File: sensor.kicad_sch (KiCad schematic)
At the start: 1 part, among them U301 AS7341DLG

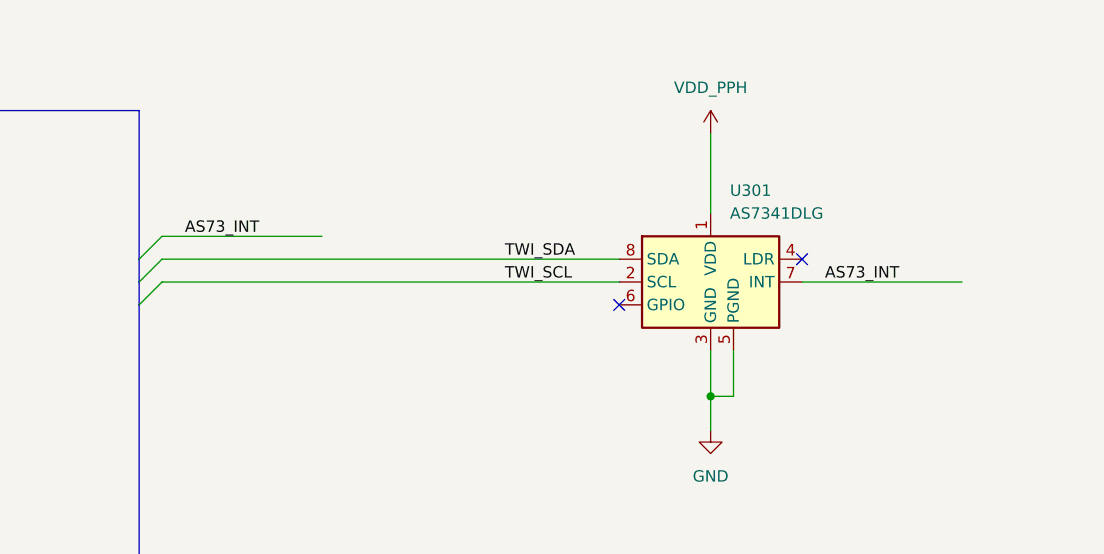
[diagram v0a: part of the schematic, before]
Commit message: Update Schematics - Add footprint to symbols.
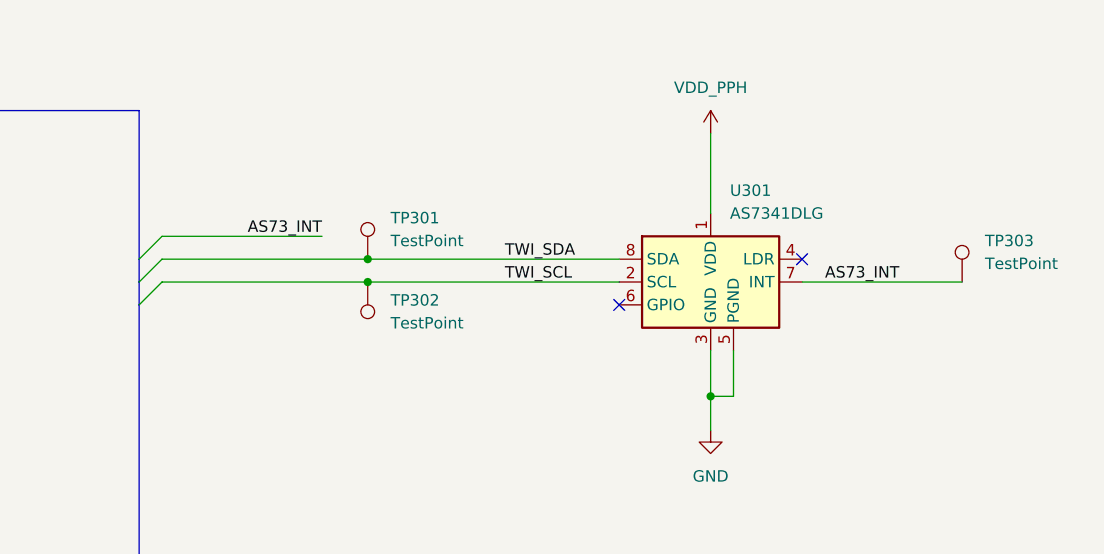
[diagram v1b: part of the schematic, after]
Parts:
- added TP301, TP302, TP303: TestPoint, TestPoint:TestPoint_Keystone_5005-5009_Compact, symbol Connector:TestPoint
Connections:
- net AS73_INT: now also TP303.1
- net TWI_SCL: now also TP302.1
- net TWI_SDA: now also TP301.1
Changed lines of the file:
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@@
+		(color 0 0 0 0)
+	)
+	(junction
+		(at 101.6 57.15)
+		(diameter 0)
+		(color 0 0 0 0)
+	)
+	(junction
+		(at 101.6 54.61)
+		(diameter 0)
 		(color 0 0 0 0)
 	)
@@
 		)
 	)
+	(wire
+		(pts
+			(xy 101.6 54.61) (xy 129.54 54.61)
+		)
+		(stroke
+			(width 0)
+			(type default)
+		)
+	)
 	(bus
 		(pts
@@
 	(wire
 		(pts
+			(xy 101.6 57.15) (xy 129.54 57.15)
+		)
+		(stroke
+			(width 0)
+			(type default)
+		)
+	)
+	(wire
+		(pts
 			(xy 26.67 33.02) (xy 39.37 33.02)
 		)
@@
 	(wire
 		(pts
-			(xy 78.74 54.61) (xy 129.54 54.61)
-		)
-		(stroke
-			(width 0)
-			(type default)
-		)
-	)
-	(wire
-		(pts
-			(xy 78.74 57.15) (xy 129.54 57.15)
+			(xy 78.74 54.61) (xy 101.6 54.61)
+		)
+		(stroke
+			(width 0)
+			(type default)
+		)
+	)
+	(wire
+		(pts
+			(xy 78.74 57.15) (xy 101.6 57.15)
 		)
 		(stroke
@@
 	)
 	(label "AS73_INT"
-		(at 81.28 52.07 0)
+		(at 96.52 52.07 180)
 		(effects
 			(font
 				(size 1.27 1.27)
 			)
-			(justify left bottom)
+			(justify right bottom)
 		)
 	)
@@
 	)
 	(symbol
+		(lib_id "Connector:TestPoint")
+		(at 101.6 54.61 0)
+		(unit 1)
+		(exclude_from_sim no)
+		(in_bom yes)
+		(on_board yes)
+		(dnp no)
+		(fields_autoplaced yes)
+		(property "Reference" "TP301"
+			(at 104.14 50.0379 0)
+			(effects
+				(font
+					(size 1.27 1.27)
+				)
+				(justify left)
+			)
+		)
+		(property "Value" "TestPoint"
+			(at 104.14 52.5779 0)
+			(effects
+				(font
+					(size 1.27 1.27)
+				)
+				(justify left)
+			)
+		)
+		(property "Footprint" "TestPoint:TestPoint_Keystone_5005-5009_Compact"
+			(at 106.68 54.61 0)
+			(effects
+				(font
+					(size 1.27 1.27)
+				)
+				(hide yes)
+			)
+		)
+		(property "Datasheet" "~"
+			(at 106.68 54.61 0)
+			(effects
+				(font
+					(size 1.27 1.27)
+				)
+				(hide yes)
+			)
+		)
+		(property "Description" "test point"
+			(at 101.6 54.61 0)
+			(effects
+				(font
+					(size 1.27 1.27)
+				)
+				(hide yes)
+			)
+		)
+		(pin "1"
+		)
+		(instances
+			(project "GreenHAir_Node"
+				(path "/0fb6cf8e-df3c-4656-9a7e-f74b2436dafb/818579d5-87db-498a-9939-a030b465af68"
+					(reference "TP301")
+					(unit 1)
+				)
+			)
+		)
+	)
+	(symbol
 		(lib_id "Sensor_Optical:AS7341DLG")
 		(at 139.7 57.15 0)
@@
 					(unit 1)
 				)
+			)
+		)
+	)
+	(symbol
+		(lib_id "Connector:TestPoint")
+		(at 167.64 57.15 0)
+		(unit 1)
+		(exclude_from_sim no)
+		(in_bom yes)
+		(on_board yes)
+		(dnp no)
+		(fields_autoplaced yes)
+		(property "Reference" "TP303"
+			(at 170.18 52.5779 0)
+			(effects
+				(font
+					(size 1.27 1.27)
+				)
+				(justify left)
+			)
+		)
+		(property "Value" "TestPoint"
+			(at 170.18 55.1179 0)
+			(effects
+				(font
+					(size 1.27 1.27)
+				)
+				(justify left)
+			)
+		)
+		(property "Footprint" "TestPoint:TestPoint_Keystone_5005-5009_Compact"
+			(at 172.72 57.15 0)
+			(effects
+				(font
+					(size 1.27 1.27)
+				)
+				(hide yes)
+			)
+		)
+		(property "Datasheet" "~"
+			(at 172.72 57.15 0)
+			(effects
+				(font
+					(size 1.27 1.27)
+				)
+				(hide yes)
+			)
+		)
+		(property "Description" "test point"
+			(at 167.64 57.15 0)
+			(effects
+				(font
+					(size 1.27 1.27)
+				)
+				(hide yes)
+			)
+		)
+		(pin "1"
+		)
+		(instances
+			(project "GreenHAir_Node"
+				(path "/0fb6cf8e-df3c-4656-9a7e-f74b2436dafb/818579d5-87db-498a-9939-a030b465af68"
+					(reference "TP303")
+					(unit 1)
+				)
+			)
+		)
+	)
+	(symbol
+		(lib_id "Connector:TestPoint")
+		(at 101.6 57.15 180)
+		(unit 1)
+		(exclude_from_sim no)
+		(in_bom yes)
+		(on_board yes)
+		(dnp no)
+		(fields_autoplaced yes)
+		(property "Reference" "TP302"
+			(at 104.14 59.1819 0)
+			(effects
+				(font
+					(size 1.27 1.27)
+				)
+				(justify right)
+			)
+		)
+		(property "Value" "TestPoint"
+			(at 104.14 61.7219 0)
+			(effects
+				(font
+					(size 1.27 1.27)
+				)
+				(justify right)
+			)
+		)
+		(property "Footprint" "TestPoint:TestPoint_Keystone_5005-5009_Compact"
+			(at 96.52 57.15 0)
+			(effects
+				(font
+					(size 1.27 1.27)
+				)
+				(hide yes)
+			)
+		)
+		(property "Datasheet" "~"
+			(at 96.52 57.15 0)
+			(effects
+				(font
+					(size 1.27 1.27)
+				)
+				(hide yes)
+			)
+		)
+		(property "Description" "test point"
+			(at 101.6 57.15 0)
+			(effects
+				(font
+					(size 1.27 1.27)
+				)
+				(hide yes)
+			)
+		)
+		(pin "1"
+		)
+		(instances
+			(project "GreenHAir_Node"
+				(path "/0fb6cf8e-df3c-4656-9a7e-f74b2436dafb/818579d5-87db-498a-9939-a030b465af68"
+					(reference "TP302")
+					(unit 1)
+				)
